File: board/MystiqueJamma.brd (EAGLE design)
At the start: 120 x 145 mm, 36 parts, among them IC1 7805, IC2 74LS245N, IC3 74LS245N, IC4 74LS245N, U1 AS6C4008-55PCN

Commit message: jamma spacing change
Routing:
- net COINCOUNTER2: track 6.75 -> 9.00 mm

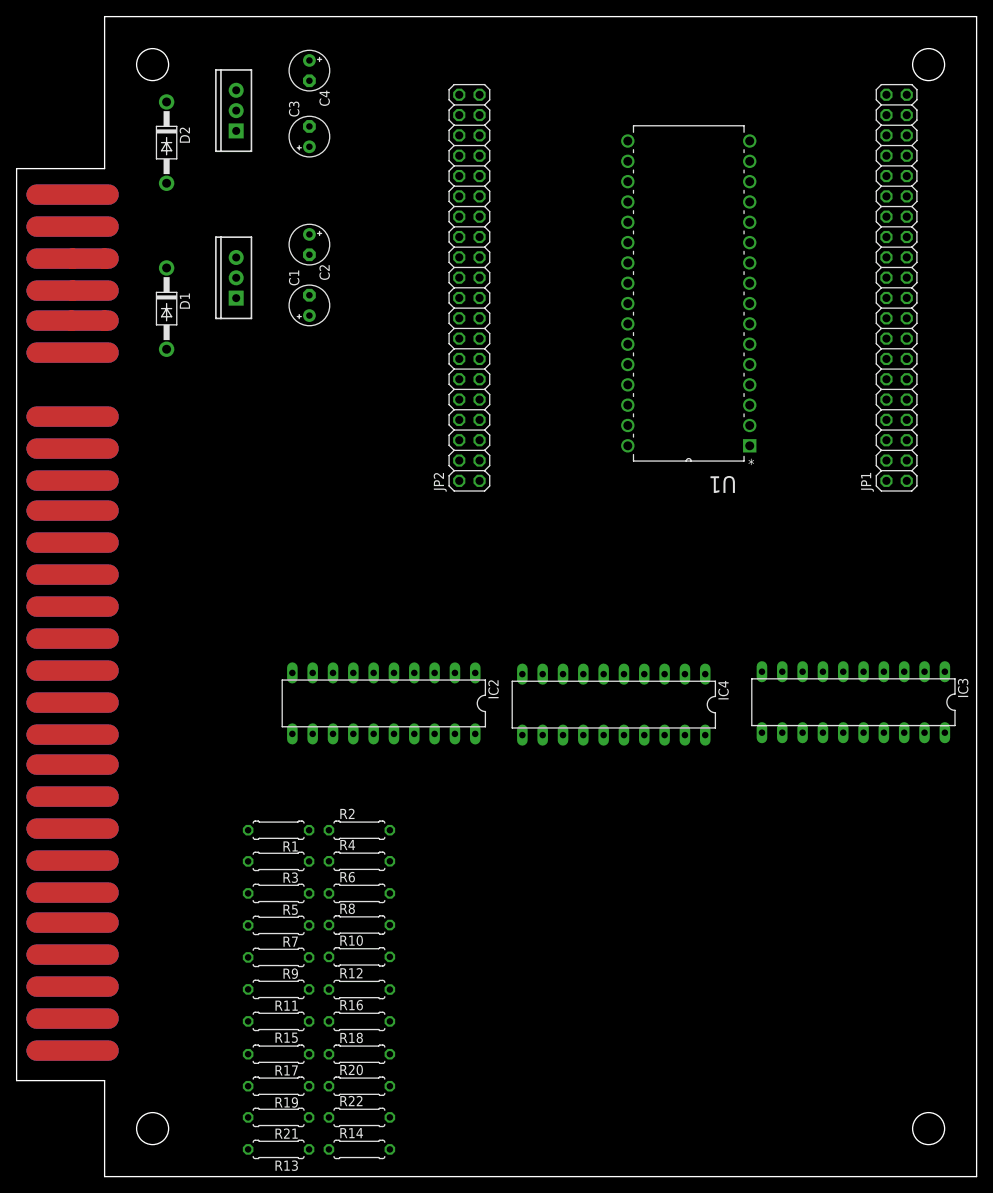
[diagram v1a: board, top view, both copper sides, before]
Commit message: included sdcard
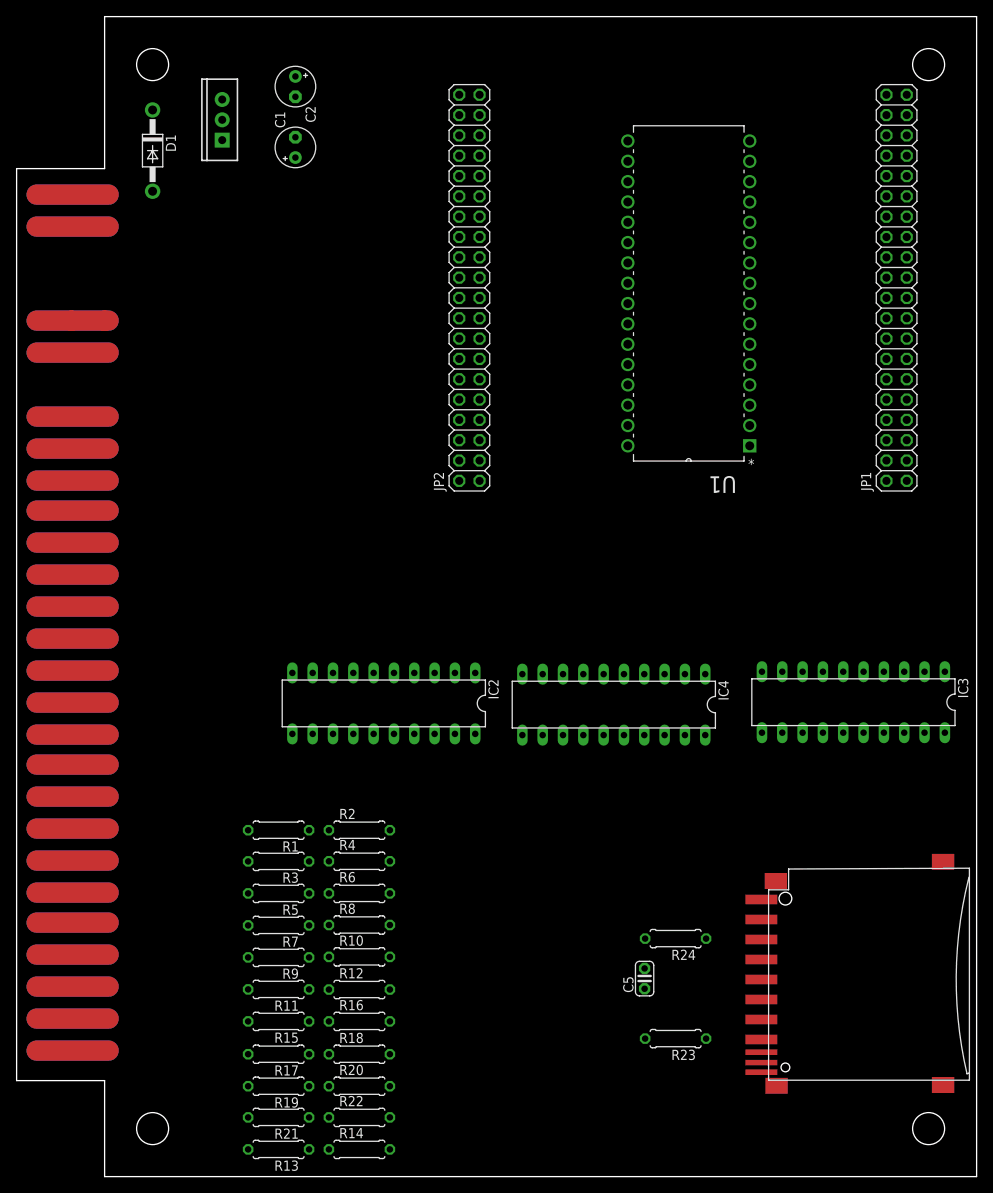
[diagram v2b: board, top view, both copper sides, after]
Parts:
- removed C3, C4: 10uF, rcl-2:E2,5-5
- removed D2: 1N4004, adafruit:DO41-10
- removed U$1: LD1117AV33, SparkFun-IC-Power:TO220-IGO
- added C5: 100nF, adafruit:C025-024X044
- added R23, R24: 10k, adafruit:0207/7
- added U$2: SDMMC06132, adafruit:06132
- moved C1 19.8 mm to (34.9, 128.7)
- moved C2 19.8 mm to (34.9, 136.2)
- moved D1 19.8 mm to (17.0, 128.2)
- moved IC1 19.8 mm to (25.7, 132.1)
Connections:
- removed net +5: D2.A
- removed net N$1: C3.+, D2.C, U$1.IN
- new net SD_CS_144: JP2.33, U$2.1
- new net SD_DATAIN_142: JP2.31, R24.1, U$2.2
- new net SD_DATAOUT_141: JP2.32, R23.1, U$2.7
- new net SD_SCLK_143: JP2.34, U$2.5
- net +3V3: now also C5.1, JP1.2, JP2.1, R23.2, R24.2, U$2.4; no longer C4.+, U$1.OUT
- net GND: now also C5.2, U$2.3, U$2.6, U$2.GP; no longer C3.-, C4.-, U$1.GND
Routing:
- net +5: track 36.0 -> 0.00 mm

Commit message: changed sram ic
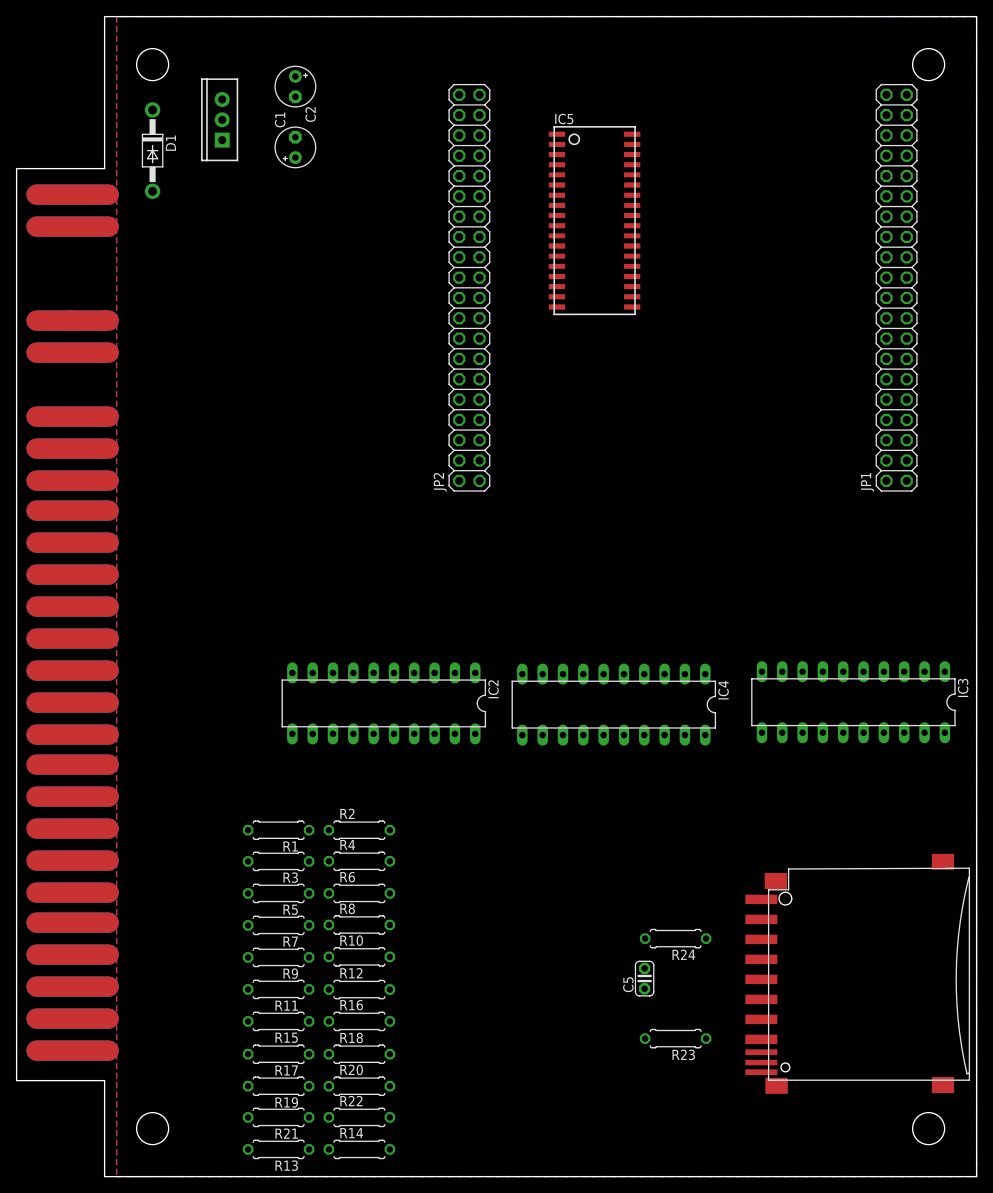
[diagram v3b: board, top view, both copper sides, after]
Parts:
- removed U1: AS6C4008-55PCN, Alliance_Memory_By_element14_Batch_1:DIP254P1524X393-32
- added IC5: CY7C1049CV33, memory-sram:SOJV36-400
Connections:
- net +3V3: now also IC5.27, IC5.9; no longer U1.32
- net GND: now also IC5.10, IC5.28; no longer U1.16
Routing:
- added copper zone on layer 1, net GND
- added copper zone on layer 16, net GND
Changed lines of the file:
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@@
 <hole x="114" y="139" drill="4"/>
 <hole x="17" y="139" drill="4"/>
-<dimension x1="108.7" y1="135.2" x2="57.9" y2="135.2" x3="83.3" y3="141.9" textsize="1.778" layer="1"/>
 <text x="156.7" y="74.8" size="1.778" layer="51">40 (30)      39 (28)
 38 (32)      37 (31)
@@
 <element name="C1" library="rcl-2" package="E2,5-5" value="10uF" x="34.85" y="128.65" rot="R90"/>
 <element name="C2" library="rcl-2" package="E2,5-5" value="10uF" x="34.85" y="136.25" rot="R270"/>
-<element name="U1" library="Alliance_Memory_By_element14_Batch_1" package="DIP254P1524X393-32" value="AS6C4008-55PCN" x="76.4" y="129.45" rot="R180">
-<attribute name="MPN" value="AS6C4008-55PCN" x="76.4" y="129.45" size="1.778" layer="27" rot="R180" display="off"/>
-<attribute name="OC_FARNELL" value="1562900" x="76.4" y="129.45" size="1.778" layer="27" rot="R180" display="off"/>
-<attribute name="OC_NEWARK" value="94M6217" x="76.4" y="129.45" size="1.778" layer="27" rot="R180" display="off"/>
-<attribute name="PACKAGE" value="DIP-32" x="76.4" y="129.45" size="1.778" layer="27" rot="R180" display="off"/>
-<attribute name="SUPPLIER" value="ALLIANCE MEMORY" x="76.4" y="129.45" size="1.778" layer="27" rot="R180" display="off"/>
-</element>
 <element name="IC2" library="74xx-us" package="DIL20" value="74LS245N" x="45.9" y="59.15" rot="R180"/>
 <element name="R1" library="adafruit" package="0207/7" value="330" x="32.75" y="43.3" rot="R180"/>
@@
 <element name="R24" library="adafruit" package="0207/7" value="10k" x="82.375" y="29.75" rot="R180"/>
 <element name="C5" library="adafruit" package="C025-024X044" value="100nF" x="78.5" y="24.75" rot="R90"/>
+<element name="IC5" library="memory-sram" package="SOJV36-400" value="CY7C1049CV33" x="72.25" y="119.5" rot="R270"/>
 </elements>
 <signals>
@@
 <contactref element="C1" pad="-"/>
 <contactref element="C2" pad="-"/>
-<contactref element="U1" pad="16"/>
 <contactref element="IC2" pad="10"/>
 <contactref element="IC2" pad="1"/>
@@
 <contactref element="U$2" pad="3"/>
 <contactref element="C5" pad="2"/>
-<wire x1="108.73" y1="114.91" x2="111.27" y2="114.91" width="0" layer="19" extent="1-1"/>
-<wire x1="91.64" y1="129.45" x2="108.73" y2="114.91" width="0" layer="19" extent="1-1"/>
-<wire x1="57.87" y1="114.91" x2="91.64" y2="129.45" width="0" layer="19" extent="1-1"/>
-<wire x1="55.33" y1="114.91" x2="57.87" y2="114.91" width="0" layer="19" extent="1-1"/>
-<wire x1="34.85" y1="129.92" x2="55.33" y2="114.91" width="0" layer="19" extent="1-1"/>
-<wire x1="34.85" y1="134.98" x2="34.85" y2="129.92" width="0" layer="19" extent="1-1"/>
-<wire x1="25.7" y1="132.1" x2="34.85" y2="129.92" width="0" layer="19" extent="1-1"/>
-<wire x1="11.5" y1="122.75" x2="25.7" y2="132.1" width="0" layer="19" extent="1-1"/>
+<contactref element="IC5" pad="10"/>
+<contactref element="IC5" pad="28"/>
+<polygon width="0.1524" layer="1">
+<vertex x="12.5" y="145"/>
+<vertex x="12.5" y="0"/>
+<vertex x="20.25" y="0"/>
+<vertex x="120" y="0"/>
+<vertex x="120" y="145"/>
+<vertex x="109.25" y="145"/>
+</polygon>
+<polygon width="0.1524" layer="16">
+<vertex x="12.5" y="145"/>
+<vertex x="12.5" y="0"/>
+<vertex x="14.25" y="0"/>
+<vertex x="120" y="0"/>
+<vertex x="120" y="2"/>
+<vertex x="120" y="145"/>
+<vertex x="114.75" y="145"/>
+</polygon>
 <wire x1="11.5" y1="122.75" x2="11.5" y2="122.75" width="0" layer="19" extent="1-16"/>
 <wire x1="11.5" y1="118.75" x2="11.5" y2="122.75" width="0" layer="19" extent="1-1"/>
 <wire x1="11.5" y1="118.75" x2="11.5" y2="118.75" width="0" layer="19" extent="1-16"/>
-<wire x1="57.33" y1="62.96" x2="57.87" y2="114.91" width="0" layer="19" extent="1-1"/>
-<wire x1="63.22" y1="62.81" x2="57.33" y2="62.96" width="0" layer="19" extent="1-1"/>
-<wire x1="54.79" y1="55.34" x2="57.33" y2="62.96" width="0" layer="19" extent="1-1"/>
-<wire x1="83.54" y1="55.19" x2="63.22" y2="62.81" width="0" layer="19" extent="1-1"/>
-<wire x1="86.08" y1="62.81" x2="83.54" y2="55.19" width="0" layer="19" extent="1-1"/>
-<wire x1="93.17" y1="63.11" x2="86.08" y2="62.81" width="0" layer="19" extent="1-1"/>
-<wire x1="113.49" y1="55.49" x2="93.17" y2="63.11" width="0" layer="19" extent="1-1"/>
-<wire x1="116.03" y1="63.11" x2="113.49" y2="55.49" width="0" layer="19" extent="1-1"/>
-<wire x1="34.47" y1="62.96" x2="54.79" y2="55.34" width="0" layer="19" extent="1-1"/>
-<wire x1="78.5" y1="26.02" x2="83.54" y2="55.19" width="0" layer="19" extent="1-1"/>
-<wire x1="93.1" y1="27.15" x2="78.5" y2="26.02" width="0" layer="19" extent="1-1"/>
-<wire x1="93.1" y1="19.65" x2="93.1" y2="27.15" width="0" layer="19" extent="1-1"/>
-<wire x1="115.8" y1="11.45" x2="93.1" y2="19.65" width="0" layer="19" extent="1-1"/>
+<wire x1="25.7" y1="132.1" x2="11.5" y2="122.75" width="0" layer="19" extent="1-1"/>
 <wire x1="11.5" y1="19.75" x2="34.47" y2="62.96" width="0" layer="19" extent="1-1"/>
 <wire x1="2.5" y1="19.75" x2="2.5" y2="19.75" width="0" layer="19" extent="1-16"/>
@@
 </signal>
 <signal name="+3V3">
-<contactref element="U1" pad="32"/>
 <contactref element="R2" pad="2"/>
 <contactref element="R4" pad="2"/>
@@
 <contactref element="JP1" pad="2"/>
 <contactref element="JP2" pad="1"/>
-<wire x1="76.4" y1="91.35" x2="108.73" y2="86.97" width="0" layer="19" extent="1-1"/>
-<wire x1="57.87" y1="86.97" x2="76.4" y2="91.35" width="0" layer="19" extent="1-1"/>
+<contactref element="IC5" pad="9"/>
+<contactref element="IC5" pad="27"/>
+<wire x1="76.949" y1="118.865" x2="108.73" y2="86.97" width="0" layer="19" extent="1-1"/>
+<wire x1="67.551" y1="120.135" x2="76.949" y2="118.865" width="0" layer="19" extent="1-1"/>
+<wire x1="57.87" y1="86.97" x2="67.551" y2="120.135" width="0" layer="19" extent="1-1"/>
 <wire x1="46.66" y1="43.2999875" x2="57.87" y2="86.97" width="0" layer="19" extent="1-1"/>
 <wire x1="46.66" y1="39.41665625" x2="46.66" y2="43.2999875" width="0" layer="19" extent="1-1"/>
